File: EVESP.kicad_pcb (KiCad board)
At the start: 2 copper layers, 103 parts, among them J1 Screw_Terminal_01x08, J2 Screw_Terminal_01x10, J3 Conn_01x04, J4 Conn_01x16_Male, J5 Conn_01x16_Female, J6 Conn_01x20_Female, J7 Conn_01x20_Male, J8 Screw_Terminal_01x03, J9 Screw_Terminal_01x03, Q1 BC847, Q2 BC847, U1 LM7332, U2 MOC3063M, U3 MOC3063M, U4 MOC3063M

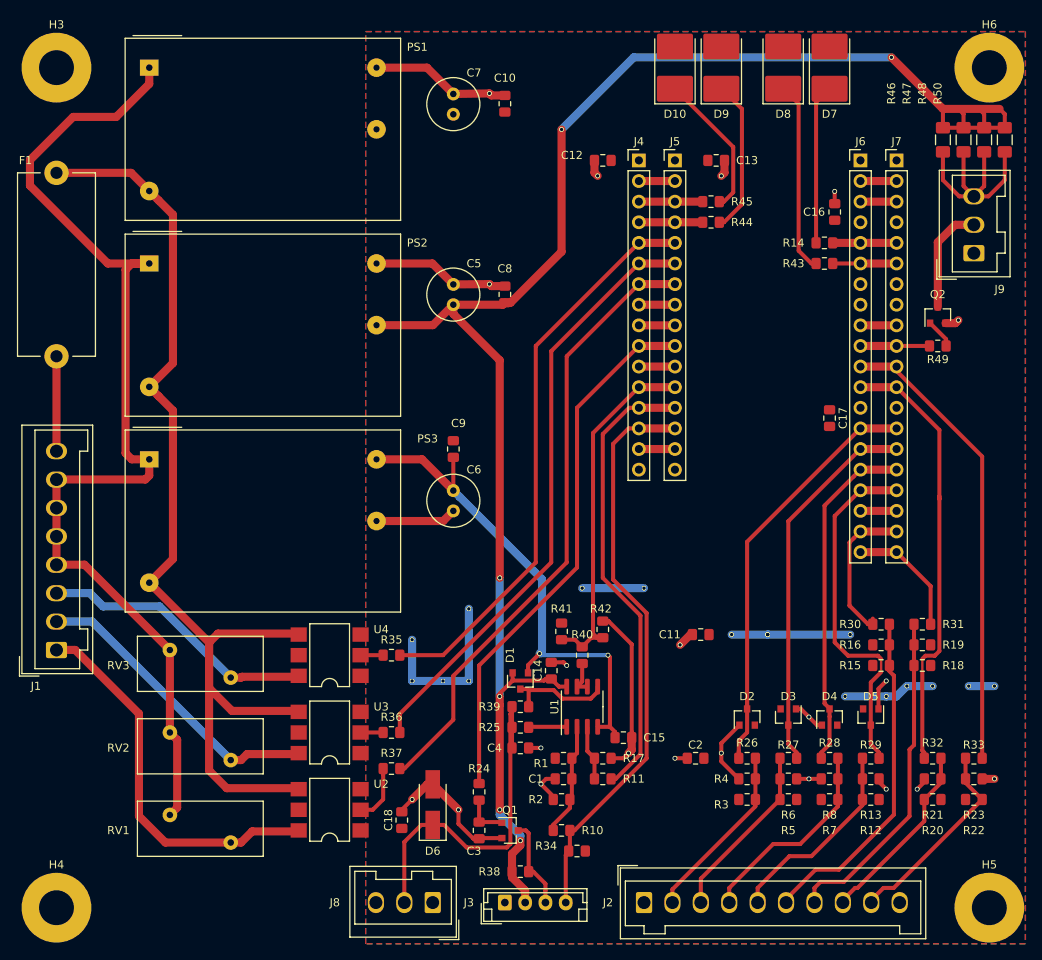
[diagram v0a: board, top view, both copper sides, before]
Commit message: Only 4 external LEDs. Smaller layout.
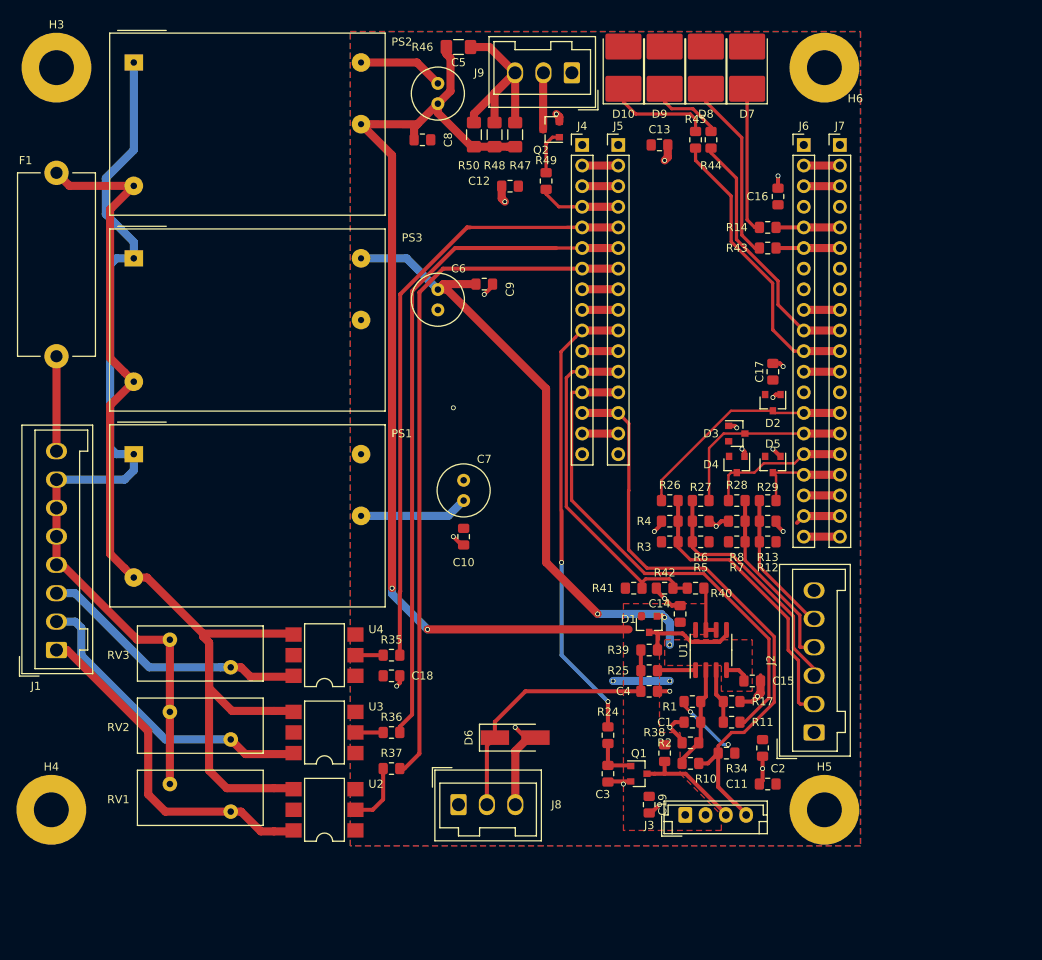
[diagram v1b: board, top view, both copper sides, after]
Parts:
- removed R15, R16, R18, R19, R20, R21, R22, R23: 10k, Resistor_SMD:R_0805_2012Metric_Pad1.15x1.40mm_HandSolder
- removed R30, R31, R32, R33: 470R, Resistor_SMD:R_0805_2012Metric_Pad1.15x1.40mm_HandSolder
- added C19: 100n, Resistor_SMD:R_0805_2012Metric_Pad1.15x1.40mm_HandSolder, F.Cu at (120.0, 158.1)
- J2: value Screw_Terminal_01x10 -> Screw_Terminal_01x06; footprint Connector_Wago:Wago_734-140_1x10_P3.50mm_Vertical -> Connector_Wago:Wago_734-136_1x06_P3.50mm_Vertical
- moved R50 65.4 mm to (98.4, 75.6), turned to 90 degrees
- moved R46 60.8 mm to (96.5, 64.8), turned to 0 degrees
- moved R48 60.3 mm to (101.0, 75.6), turned to 90 degrees
- moved R47 55.2 mm to (103.5, 75.6), turned to 90 degrees
- moved J9 54.3 mm to (110.5, 67.9), turned to 180 degrees
- moved C10 53.6 mm to (97.2, 125.1), turned to 270 degrees
- moved Q2 52.8 mm to (108.0, 74.9), turned to 180 degrees
- moved R49 52.4 mm to (107.3, 81.3), turned to 270 degrees
- moved PS1 47.7 mm to (56.5, 114.9)
- moved C7 47.6 mm to (97.2, 120.7)
- moved D2 38.9 mm to (135.3, 108.6), turned to 270 degrees
- moved D3 35.5 mm to (130.8, 112.4), turned to 0 degrees
- moved R13 34.2 mm to (134.6, 123.2)
- moved R29 34.2 mm to (134.6, 120.7)
- moved R12 34.2 mm to (134.6, 125.7)
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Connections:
- net /D4 renamed Net-(J6-Pad19)
- net /D5 renamed Net-(J6-Pad20)
- net /D6 renamed Net-(J6-Pad12)
- J2 pad 6: Net-(J2-Pad6) -> GND
- J4 pad 3: /LED0_n -> Net-(J4-Pad3)
- J4 pad 4: /LED1_n -> /Light_n
- J5 pad 3: /LED0_n -> Net-(J4-Pad3)
- J5 pad 4: /LED1_n -> /Light_n
- J6 pad 10: /Light_n -> /LED1_n
- J6 pad 11: /D7 -> /LED0_n
- J7 pad 10: /Light_n -> /LED1_n
- J7 pad 11: /D7 -> /LED0_n
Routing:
- net +12V: track 215.5 -> 123.4 mm, vias 6 -> 2
- net /D7: track 61.2 -> 0.00 mm
- net GND: track 130.3 -> 75.9 mm, vias 21 -> 23
- net Net-(J6-Pad12): track 54.2 -> 4.44 mm
- net Net-(J2-Pad6): track 41.7 -> 0.00 mm
- net Net-(J2-Pad7): track 41.1 -> 0.00 mm
- net (no net): track 36.7 -> 0.00 mm, vias 12 -> 0
- net /D3: track 44.3 -> 12.0 mm
- net /LED0_n: track 7.86 -> 39.6 mm
- net /D1: track 53.5 -> 27.2 mm
- net Net-(J2-Pad9): track 25.0 -> 0.00 mm
- net /D0: track 57.0 -> 32.0 mm
- net /D2: track 42.5 -> 17.9 mm
- net /LED1_n: track 7.86 -> 31.6 mm
- net Net-(J2-Pad8): track 23.0 -> 0.00 mm
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- added copper zone on F.Cu, net +12V
- added copper zone on F.Cu, net -12V
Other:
- net class 240Vac: clearance 1.27 -> 0.508

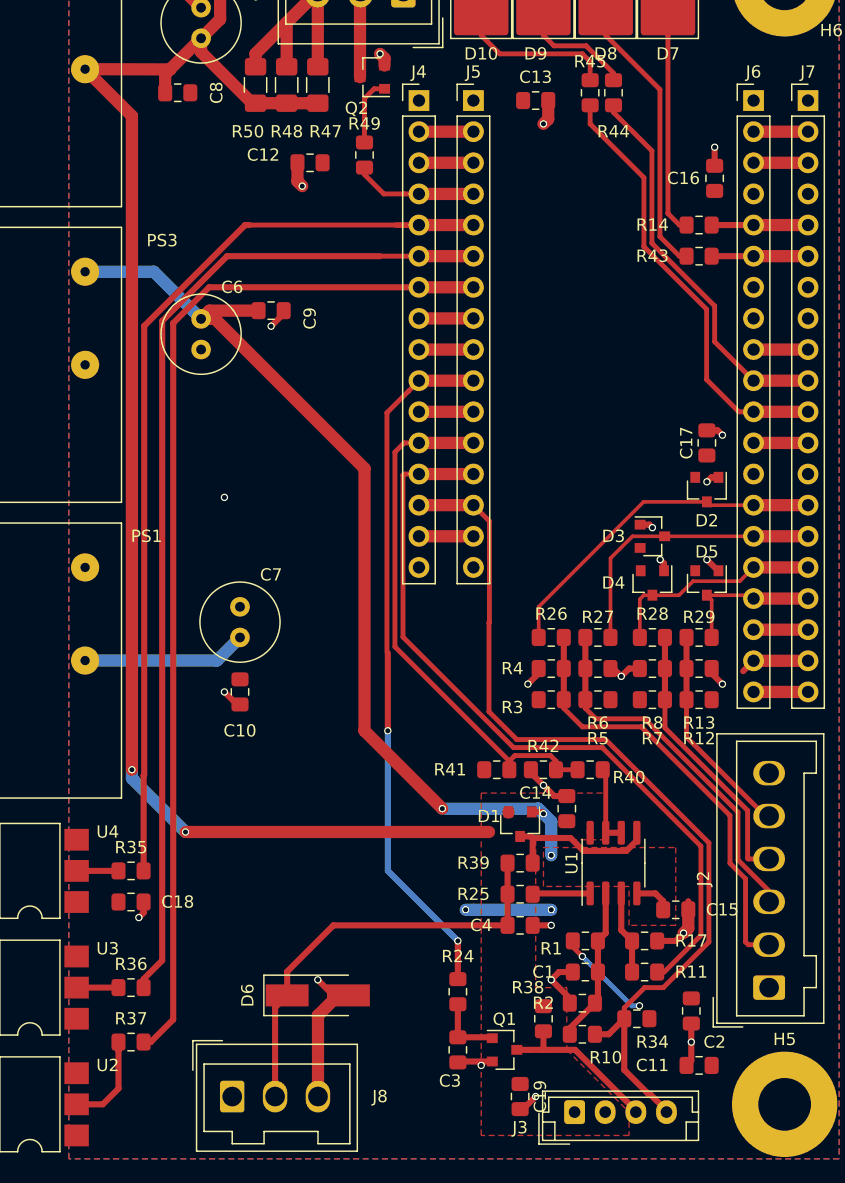
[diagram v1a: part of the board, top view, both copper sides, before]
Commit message: Added analog protection against disconnect and diode failure on car side.
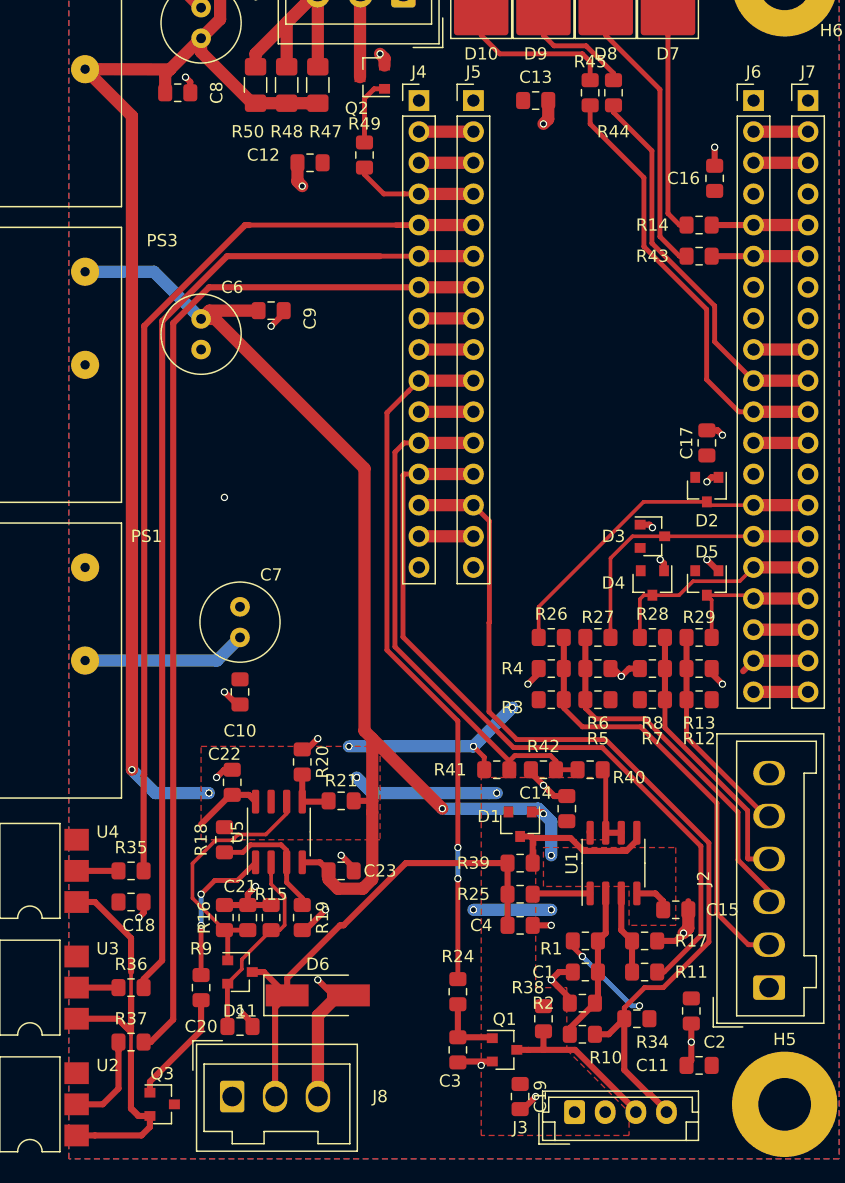
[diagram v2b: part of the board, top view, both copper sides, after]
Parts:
- added C20: 100n, Resistor_SMD:R_0805_2012Metric_Pad1.15x1.40mm_HandSolder, F.Cu at (97.2, 152.4)
- added C21: 100n, Resistor_SMD:R_0805_2012Metric_Pad1.15x1.40mm_HandSolder, F.Cu at (97.8, 143.5)
- added C22: 100n, Capacitor_SMD:C_0805_2012Metric_Pad1.15x1.40mm_HandSolder, F.Cu at (96.5, 132.5)
- added C23: 100n, Capacitor_SMD:C_0805_2012Metric_Pad1.15x1.40mm_HandSolder, F.Cu at (105.4, 139.7)
- added D11: BAT54S, Package_TO_SOT_SMD:SOT-23, F.Cu at (97.2, 148.0)
- added Q3: BC847, Package_TO_SOT_SMD:SOT-23, F.Cu at (90.8, 158.8)
- added R15: 1M, Resistor_SMD:R_0805_2012Metric_Pad1.15x1.40mm_HandSolder, F.Cu at (99.7, 143.5)
- added R16: 1M, Resistor_SMD:R_0805_2012Metric_Pad1.15x1.40mm_HandSolder, F.Cu at (95.9, 143.5)
- added R18: 2k2, Resistor_SMD:R_0805_2012Metric_Pad1.15x1.40mm_HandSolder, F.Cu at (95.9, 137.2)
- added R19: 10k, Resistor_SMD:R_0805_2012Metric_Pad1.15x1.40mm_HandSolder, F.Cu at (102.2, 143.5)
- added R20: 10k, Resistor_SMD:R_0805_2012Metric_Pad1.15x1.40mm_HandSolder, F.Cu at (102.2, 130.8)
- added R21: 4k7, Resistor_SMD:R_0805_2012Metric_Pad1.15x1.40mm_HandSolder, F.Cu at (105.4, 134.0)
- added R9: 10k, Resistor_SMD:R_0805_2012Metric_Pad1.15x1.40mm_HandSolder, F.Cu at (94.0, 149.2)
- added U5: LM7332, Package_SO:SOIC-8_3.9x4.9mm_P1.27mm, F.Cu at (100.3, 136.5)
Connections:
- U2 pad 1: +3V3 -> Net-(Q3-Pad2)
- U3 pad 1: +3V3 -> Net-(Q3-Pad2)
- U4 pad 1: +3V3 -> Net-(Q3-Pad2)
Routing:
- net Net-(Q3-Pad2): track 0.00 -> 49.6 mm
- net Net-(C21-Pad1): track 0.00 -> 21.4 mm
- net -12V: track 81.0 -> 101.4 mm
- net +3V3: track 28.3 -> 44.6 mm, vias 5 -> 8
- net GND: track 75.9 -> 92.2 mm, vias 23 -> 30
- net Net-(C20-Pad1): track 0.00 -> 16.2 mm
- net /Charge: track 0.00 -> 12.1 mm, vias 0 -> 2
- net Net-(R18-Pad2): track 0.00 -> 10.5 mm
- net Net-(Q3-Pad1): track 0.00 -> 9.28 mm
- net +12V: track 123.4 -> 116.3 mm, vias 2 -> 4
- net /CP: track 35.2 -> 40.7 mm
- net Net-(R20-Pad2): track 0.00 -> 4.39 mm

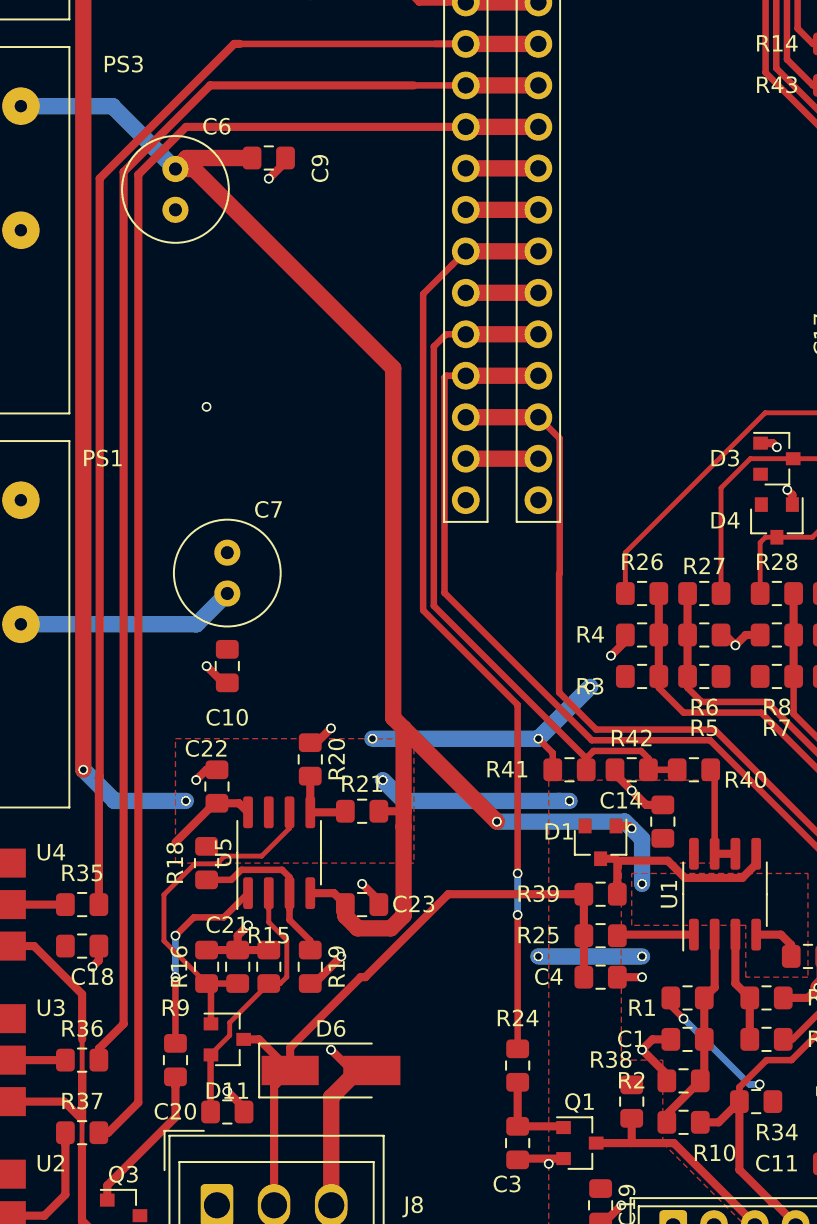
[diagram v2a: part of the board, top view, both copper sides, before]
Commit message: Added HW safety. No relay drive unless the CP is connected and RCM is happy.
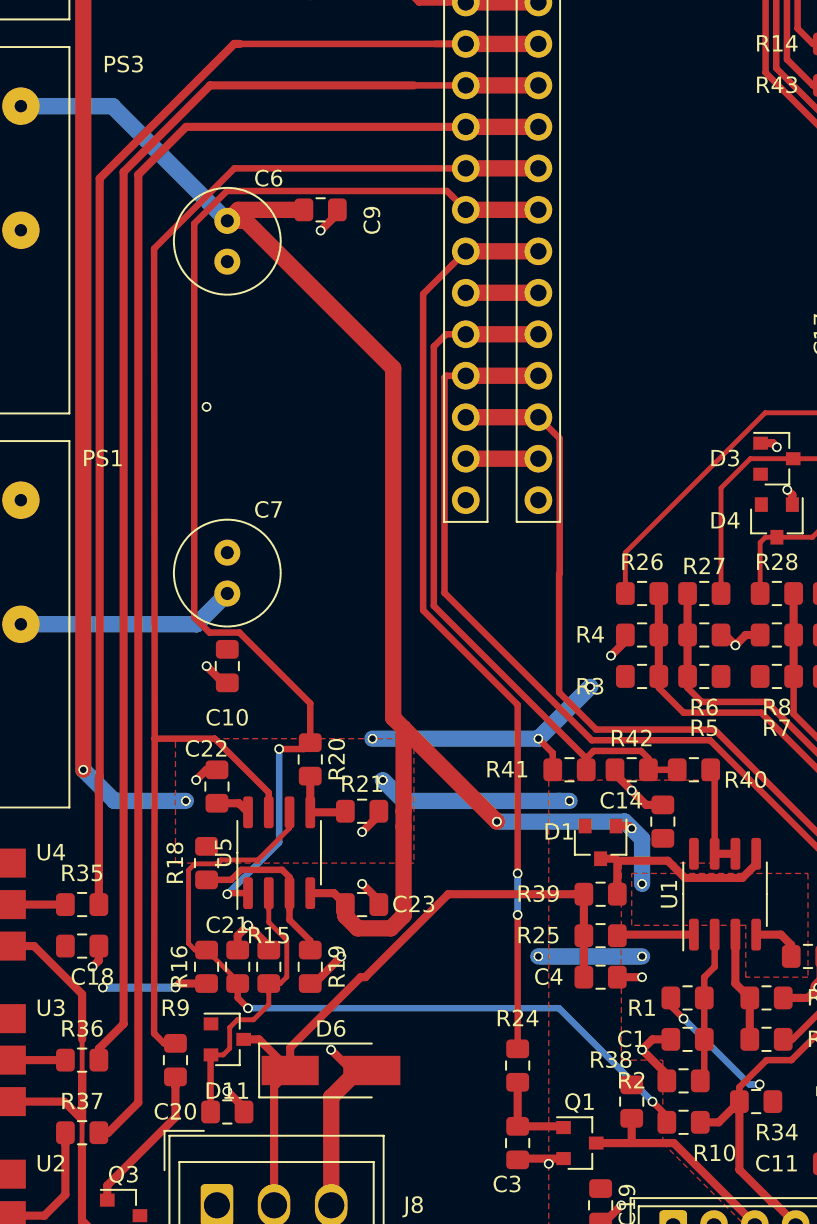
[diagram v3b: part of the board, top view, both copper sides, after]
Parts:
- R16: value 1M -> 10k
- R18: value 2k2 -> 6k8
- R21: value 4k7 -> 47k
- R34: value DNI 10k -> 10k
- moved C9 4.49 mm to (102.9, 97.2)
- moved C6 4.49 mm to (97.2, 100.3)
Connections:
- D11 pad 1: Net-(C21-Pad1) -> Net-(D11-Pad1)
- J4 pad 8: Net-(J4-Pad8) -> /SafeToCharge
- J4 pad 9: Net-(J4-Pad9) -> /Charge
- J5 pad 8: Net-(J4-Pad8) -> /SafeToCharge
- J5 pad 9: Net-(J4-Pad9) -> /Charge
- R10 pad 2: Net-(C1-Pad1) -> Net-(C21-Pad1)
- R16 pad 1: Net-(C21-Pad1) -> +3V3
- R16 pad 2: GND -> Net-(C21-Pad1)
- R20 pad 1: GND -> /Charge
- R21 pad 2: -12V -> GND
- R9 pad 1: /Charge -> /SafeToCharge
- U5 pad 7: /DiodeOk -> /SafeToCharge
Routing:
- net /SafeToCharge: track 0.00 -> 84.7 mm
- net /Charge: track 12.1 -> 71.7 mm
- net Net-(C21-Pad1): track 21.4 -> 47.4 mm, vias 0 -> 2
- net +3V3: track 44.6 -> 51.1 mm, vias 8 -> 10
- net Net-(J4-Pad9): track 4.44 -> 0.00 mm
- net Net-(J4-Pad8): track 4.44 -> 0.00 mm
- net +12V: track 116.3 -> 112.8 mm
- net Net-(C1-Pad1): track 12.7 -> 9.32 mm
- net GND: track 92.2 -> 90.4 mm
- net -12V: track 101.4 -> 99.8 mm
- net Net-(C20-Pad1): track 16.2 -> 17.2 mm
